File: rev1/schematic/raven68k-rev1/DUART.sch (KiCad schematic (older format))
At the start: 5 parts

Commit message: update schematic for rev1
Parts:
- removed C?: 0.1uF, symbol Device:C_Small
- added C? (x3): 0.1uF, symbol Device:C
- added R?: 4.7k, symbol Device:R_Small
- added U?: 74LS373, symbol 74xx:74LS373
- added U?: DS12887+, symbol custom:DS12887+
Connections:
- net +5V: now also X?.14 (Vcc), C?.1, C?.1, C?.1, R?.2, U?.1 (MOT), U?.18 (~RESET), U?.20 (VCC), U?.24 (Vcc)
- net A1: now also U?.3 (D0)
- net A2: now also U?.4 (D1)
- net A3: now also U?.7 (D2)
- net A4: now also U?.8 (D3)
- net D0: now also U?.2 (O0), U?.4 (AD0)
- net D1: now also U?.5 (AD1), U?.5 (O1)
- net D2: now also U?.6 (AD2), U?.6 (O2)
- net D3: now also U?.7 (AD3), U?.9 (O3)
- net D4: now also U?.12 (O4), U?.8 (AD4)
- net D5: now also U?.15 (O5), U?.9 (AD5)
- net D6: now also U?.10 (AD6), U?.16 (O6)
- net D7: now also U?.11 (AD7), U?.19 (O7)
- net GND: now also U?.2 (GND), U?.20 (GND), X?.7 (GND), C?.2, C?.2, C?.2, U?.1 (OE), U?.10 (GND), U?.12 (GND)
- net R~W: now also U?.15 (R/~W)
- net ~DUART_DTACK: no longer names the net of U?.9 (DTACK)
- net ~DUART_DTACK: now also R?.1
- new net A5: U?.13 (D4)
- new net A6: U?.14 (D5)
- new net A7: U?.17 (D6)
- new net A8: U?.18 (D7)
- new net NOT_AS: U?.11 (LE), U?.14 (AS)
- new net NOT_DS: U?.17 (DS)
- new net SQW: U?.23 (SQW)
- new net ~RTC_CS: U?.13 (~CS)
- new net ~RTC_IRQ: U?.19 (~IRQ)
- no-connect marks 4 -> 5
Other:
- moved on the sheet: J?, U?, X?

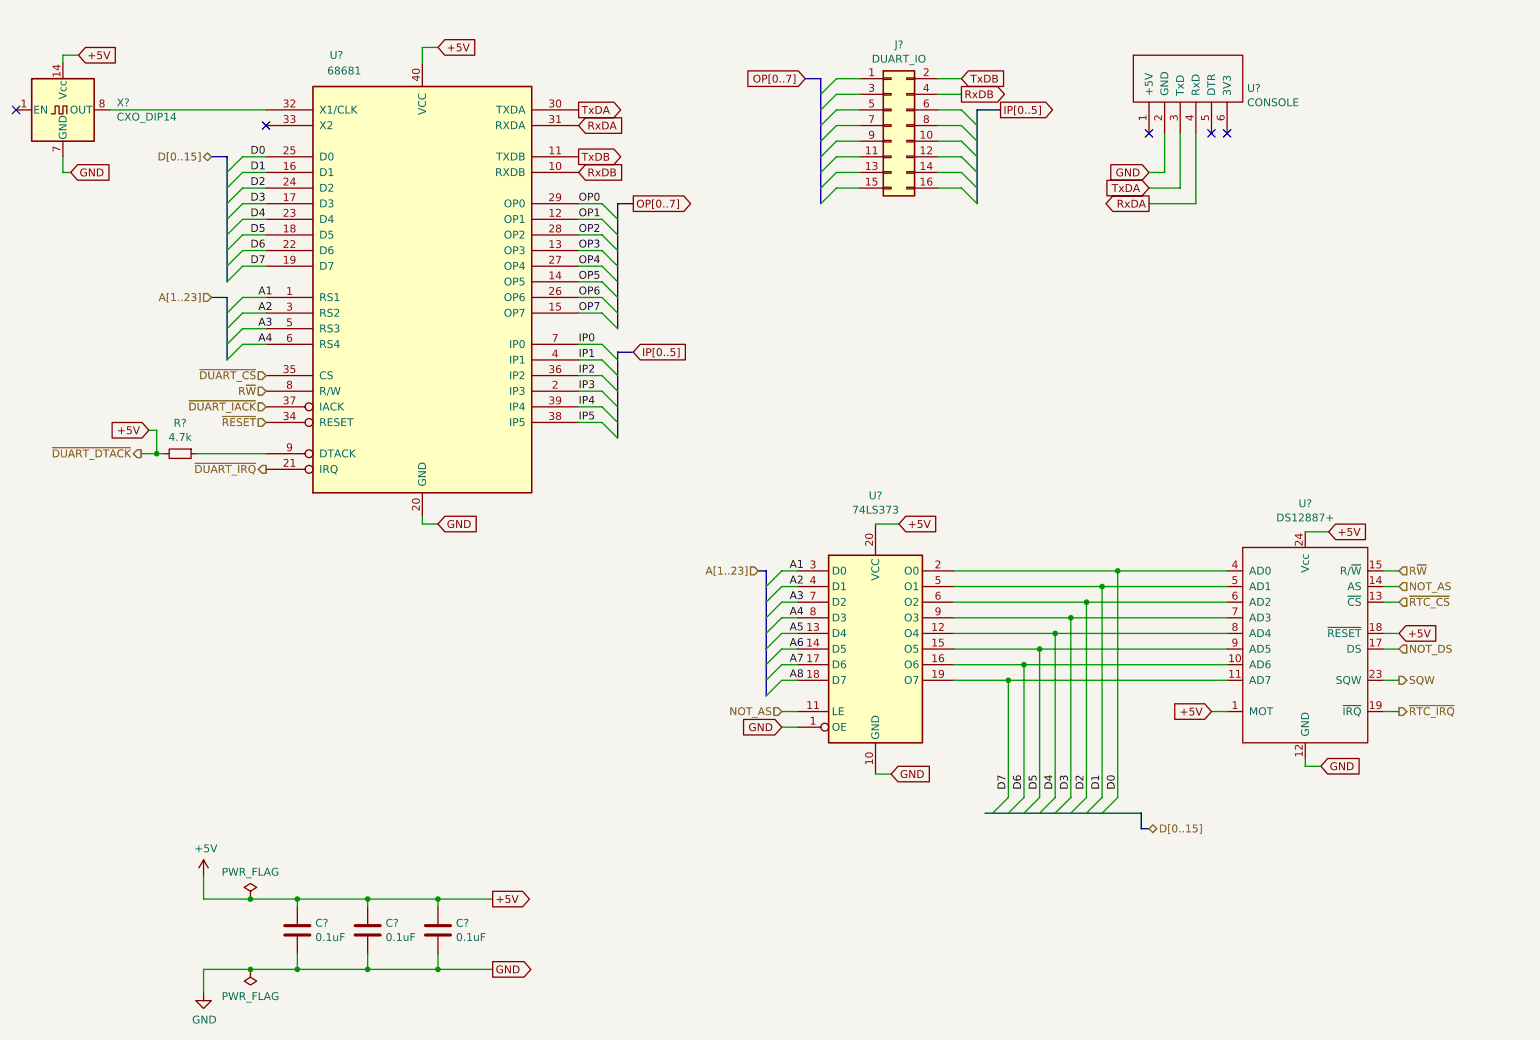
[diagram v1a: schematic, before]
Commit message: added buffers
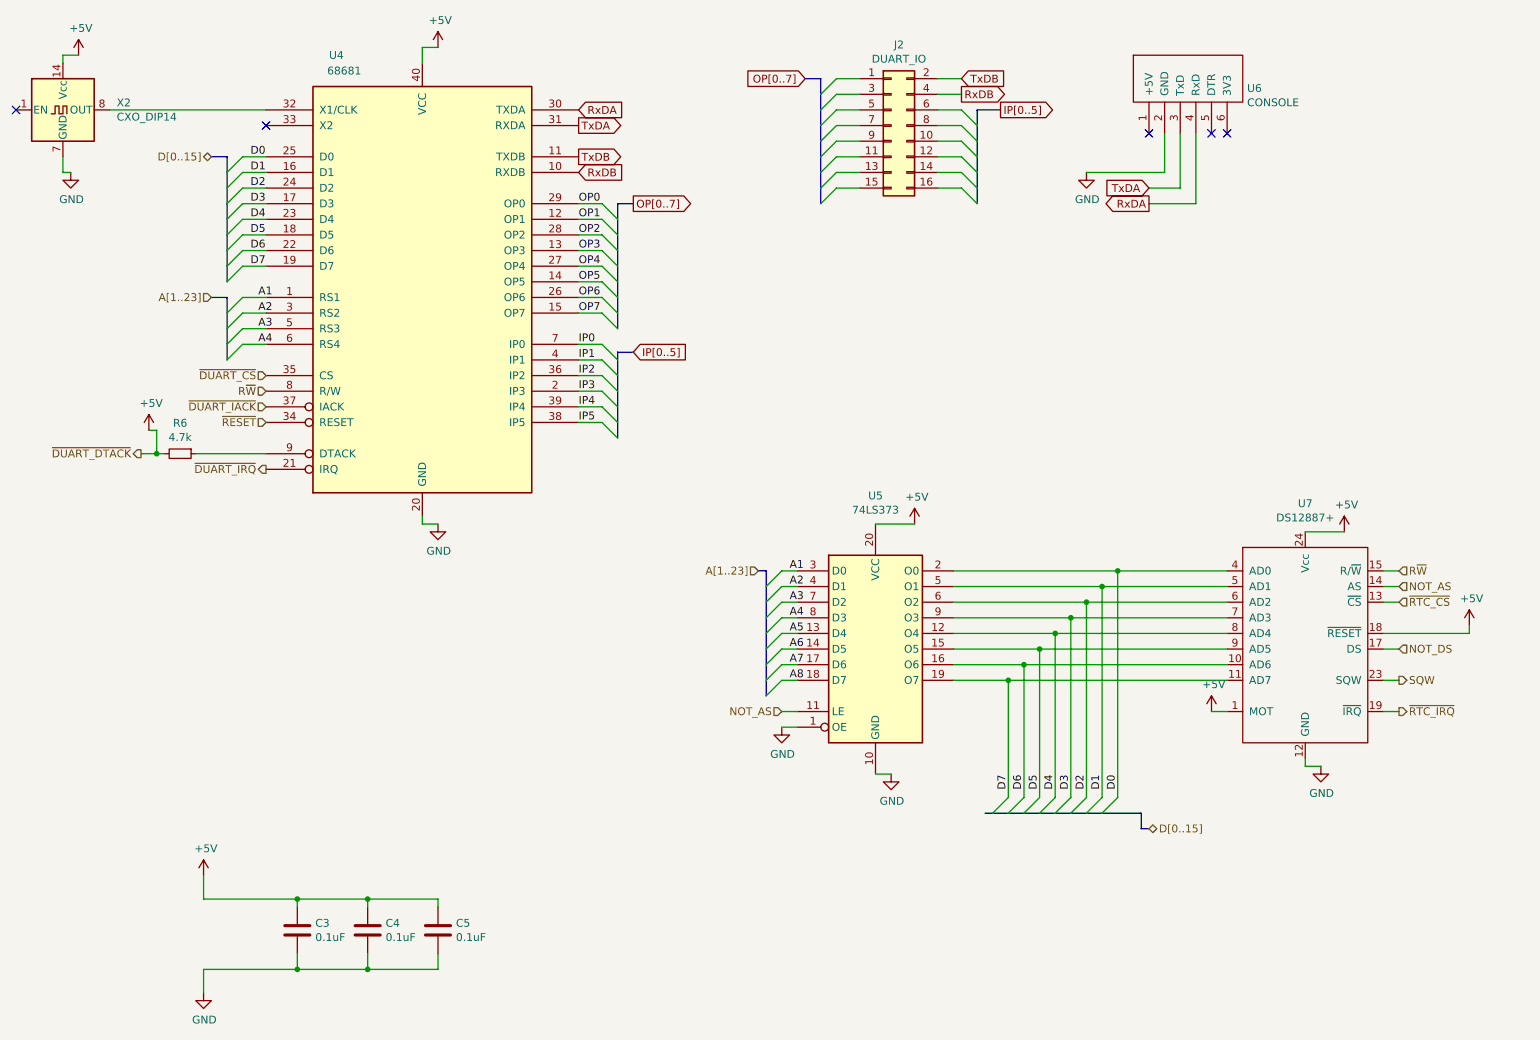
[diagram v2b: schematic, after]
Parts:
- U4: renamed from U?; footprint (none) -> Package_DIP:DIP-40_W25.4mm_Socket
- U5: renamed from U?; footprint (none) -> Package_DIP:DIP-20_W7.62mm
- U7: renamed from U?; footprint (none) -> Package_DIP:DIP-24_W7.62mm
- gave numbers to parts that had none: 7
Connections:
- net RxDA: now also U4.30 (TXDA); no longer U4.31 (RXDA)
- net TxDA: now also U4.31 (RXDA); no longer U4.30 (TXDA)

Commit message: upgrade to KiCad 6, first shot at layout
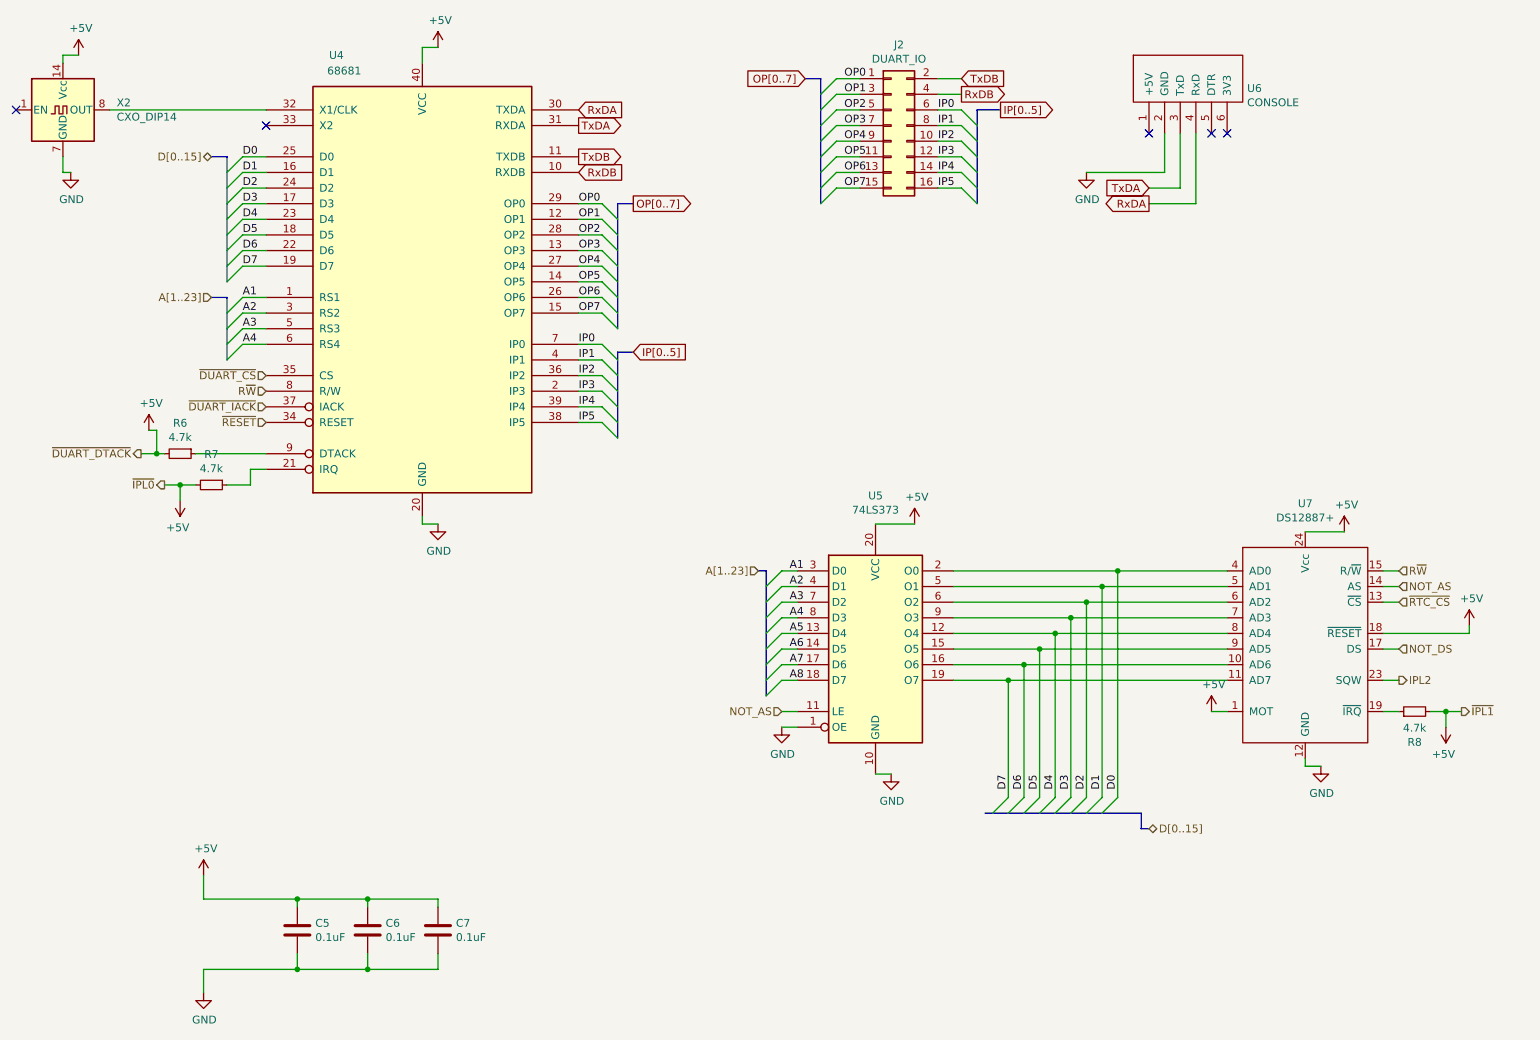
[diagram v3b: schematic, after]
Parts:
- added R7, R8: 4.7k, symbol Device:R_Small
- C5: renamed from C3; footprint (none) -> Capacitor_SMD:C_1206_3216Metric_Pad1.33x1.80mm_HandSolder
- C6: renamed from C4; footprint (none) -> Capacitor_SMD:C_1206_3216Metric_Pad1.33x1.80mm_HandSolder
- C7: renamed from C5; footprint (none) -> Capacitor_SMD:C_1206_3216Metric_Pad1.33x1.80mm_HandSolder
- J2: footprint (none) -> Connector_PinHeader_2.54mm:PinHeader_2x08_P2.54mm_Vertical
- U4: footprint Package_DIP:DIP-40_W25.4mm_Socket -> Package_DIP:DIP-40_W25.4mm_Socket_LongPads
- U5: footprint Package_DIP:DIP-20_W7.62mm -> Package_DIP:DIP-20_W7.62mm_Socket_LongPads
- U6: footprint Connector_PinHeader_1.00mm:PinHeader_1x06_P1.00mm_Vertical -> Connector_PinHeader_2.54mm:PinHeader_1x06_P2.54mm_Vertical
- U7: footprint Package_DIP:DIP-24_W7.62mm -> Package_DIP:DIP-24_W15.24mm_Socket_LongPads
- X2: footprint Oscillator:Oscillator_DIP-14 -> Oscillator:Oscillator_DIP-14_LargePads
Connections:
- net +5V: now also R7.2, R8.2
- net IP0: now also J2.6 (Pin_6)
- net IP1: now also J2.8 (Pin_8)
- net IP2: now also J2.10 (Pin_10)
- net IP3: now also J2.12 (Pin_12)
- net IP4: now also J2.14 (Pin_14)
- net IP5: now also J2.16 (Pin_16)
- net OP0: now also J2.1 (Pin_1)
- net OP1: now also J2.3 (Pin_3)
- net OP2: now also J2.5 (Pin_5)
- net OP3: now also J2.7 (Pin_7)
- net OP4: now also J2.9 (Pin_9)
- net OP5: now also J2.11 (Pin_11)
- net OP6: now also J2.13 (Pin_13)
- net OP7: now also J2.15 (Pin_15)
- net SQW renamed IPL2
- net ~DUART_IRQ: no longer names the net of U4.21 (IRQ)
- net ~DUART_IRQ: now also R7.1
- net ~RTC_IRQ: no longer names the net of U7.19 (~IRQ)
- net ~RTC_IRQ: now also R8.1
